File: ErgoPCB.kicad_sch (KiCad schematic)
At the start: 19 parts, among them J1 Conn_01x04_MountingPin, U1 STM32F072CBT6, U3 PRTR5V0U2X, U4 XC6206PxxxMR-Regulator_Linear

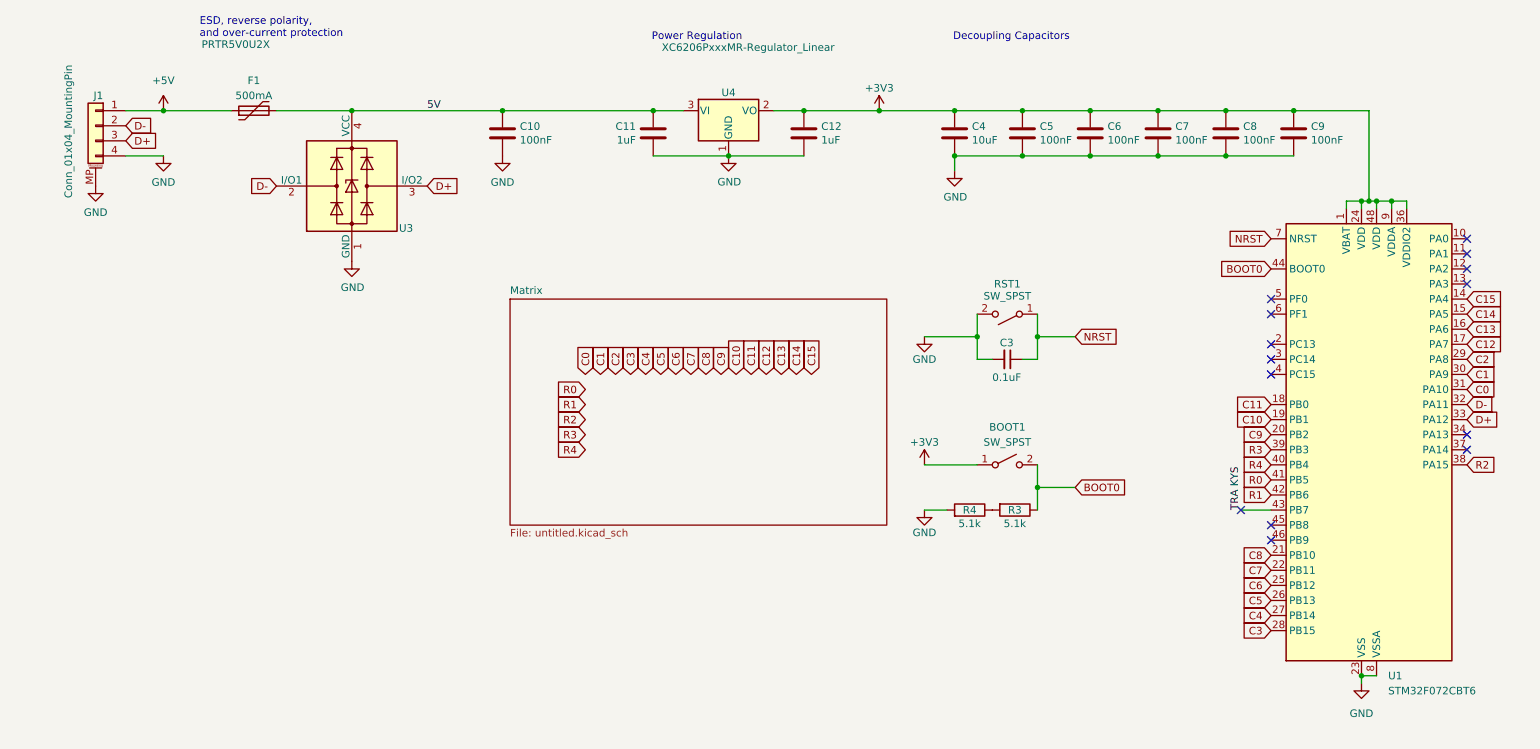
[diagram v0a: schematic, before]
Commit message: ESD protection change and redid decoupling capacitors
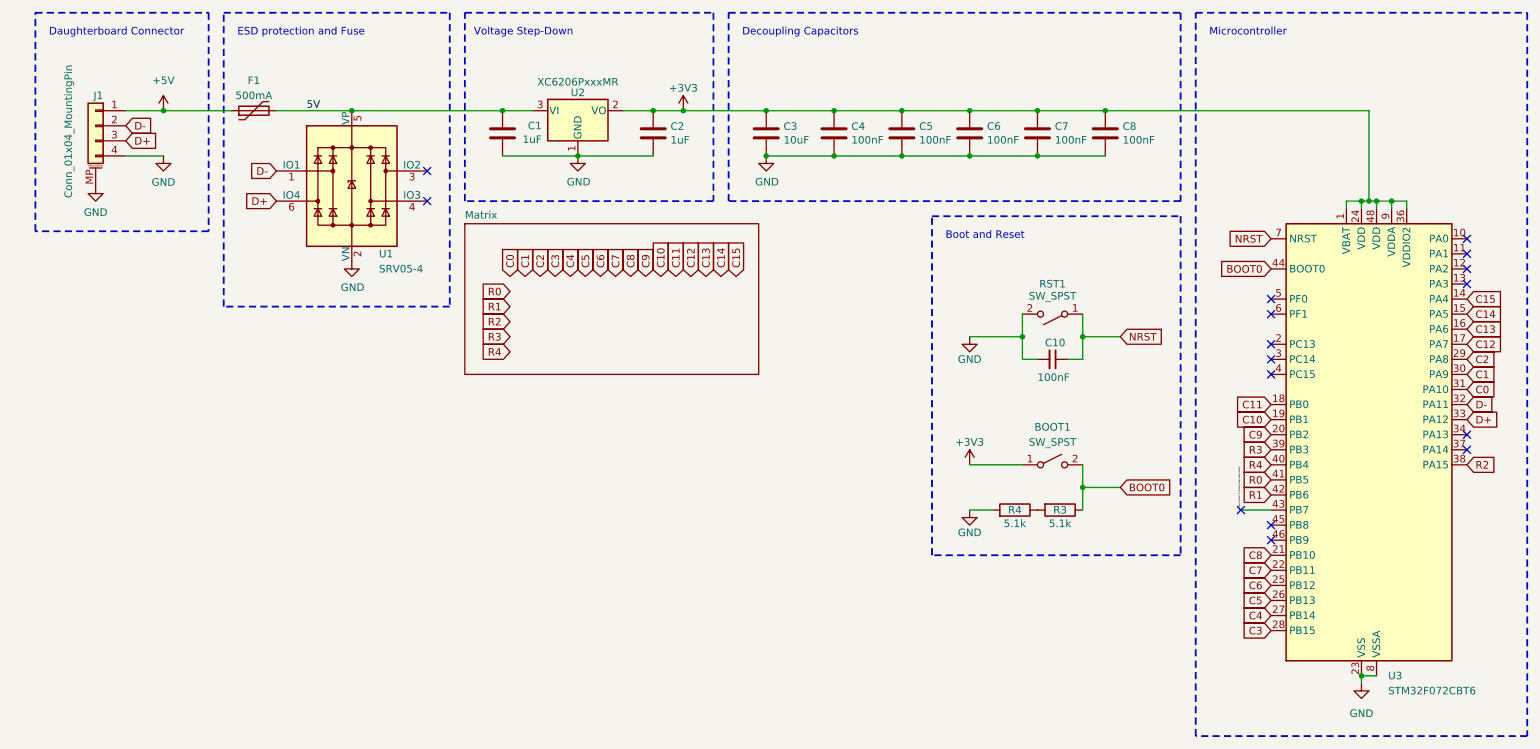
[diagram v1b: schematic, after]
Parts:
- removed C10: 100nF, Capacitor_SMD:C_0402_1005Metric, symbol Device:C
- removed U3: PRTR5V0U2X, Package_TO_SOT_SMD:SOT-143, symbol Power_Protection:PRTR5V0U2X
- added U1: SRV05-4, PCM_marbastlib-various:SOT-23-6-routable, symbol PCM_marbastlib-various:SRV05-4
- C10: renamed from C3; value 0.1uF -> 100nF
- U2: renamed from U4; value XC6206PxxxMR-Regulator_Linear -> XC6206PxxxMR
- renumbered C11 to C1, C12 to C2, C4 to C3, C5 to C4, C6 to C5, C7 to C6, C8 to C7, C9 to C8, U1 to U3
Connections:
- net 5V: now also U1.5 (VP)
- net D+: now also U1.6 (IO4)
- net D-: now also U1.1 (IO1)
- net GND: now also U1.2 (VN)
- net TRA KYS renamed pls dont connect to randon things again thanks
- no-connect marks 14 -> 16
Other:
- sheet Matrix: file untitled.kicad_sch -> Matrix.kicad_sch
- note added: "Boot and Reset"
- note added: "Daughterboard Connector"
- note added: "ESD protection and Fuse"
- note added: "Microcontroller"
- note added: "Voltage Step-Down"
- note removed: "ESD, reverse polarity, and over-current protection"
- note removed: "Power Regulation"
- moved on the sheet: BOOT1, C1, C10, C2, C3, C4, C5, C6, C7, C8, R3, R4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

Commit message: Small changes
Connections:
- net pls dont connect to randon things again thanks renamed     pls dont connect to randon things again thanks
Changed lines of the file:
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@@
 	)
 	(no_connect
-		(at 226.06 111.76)
+		(at 222.25 111.76)
 	)
 	(no_connect
@@
 	(wire
 		(pts
-			(xy 248.92 59.69) (xy 248.92 60.96)
+			(xy 222.25 111.76) (xy 231.14 111.76)
 		)
 		(stroke
@@
 	(wire
 		(pts
-			(xy 199.39 107.95) (xy 199.39 111.76)
+			(xy 248.92 59.69) (xy 248.92 60.96)
 		)
 		(stroke
@@
 	(wire
 		(pts
-			(xy 189.23 86.36) (xy 189.23 82.55)
+			(xy 199.39 107.95) (xy 199.39 111.76)
 		)
 		(stroke
@@
 	(wire
 		(pts
-			(xy 38.1 52.07) (xy 44.45 52.07)
+			(xy 189.23 86.36) (xy 189.23 82.55)
 		)
 		(stroke
@@
 	(wire
 		(pts
-			(xy 251.46 59.69) (xy 251.46 60.96)
+			(xy 38.1 52.07) (xy 44.45 52.07)
 		)
 		(stroke
@@
 	(wire
 		(pts
-			(xy 191.77 44.45) (xy 203.2 44.45)
+			(xy 251.46 59.69) (xy 251.46 60.96)
 		)
 		(stroke
@@
 	(wire
 		(pts
-			(xy 226.06 111.76) (xy 231.14 111.76)
+			(xy 191.77 44.45) (xy 203.2 44.45)
 		)
 		(stroke
@@
 		)
 	)
-	(label "pls dont connect to randon things again thanks"
-		(at 226.06 111.76 90)
+	(label "    pls dont connect to randon things again thanks"
+		(at 223.52 111.76 90)
 		(effects
 			(font
@@
 	)
 	(sheet
-		(at 95.25 63.5)
+		(at 95.25 62.23)
 		(size 49.53 25.4)
-		(fields_autoplaced yes)
 		(stroke
 			(width 0.15)
@@
 		)
 		(property "Sheetname" "Matrix"
-			(at 95.25 62.7884 0)
+			(at 96.266 66.04 0)
 			(effects
 				(font
@@
 		)
 		(property "Sheetfile" "Matrix.kicad_sch"
-			(at 95.25 89.4846 0)
+			(at 95.25 88.2146 0)
 			(effects
 				(font

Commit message: Small fixes
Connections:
- net 5V is gone; now on net +5V: C1.1, F1.2, U1.5 (VP), U2.3 (VI)
- net +5V: no longer F1.1, J1.1 (Pin_1)
- net D+: now also U1.3 (IO2), U1.4 (IO3); no longer U1.6 (IO4)
- net D-: now also U1.6 (IO4)
- new net VBUS: F1.1, J1.1 (Pin_1)
- no-connect marks 16 -> 14
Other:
- moved on the sheet: F1, J1, U1

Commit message: New molex connector footprint and 3V3 line to BOOT0 routed away from the BOOT and NRST traces
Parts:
- J1: footprint PCM_marbastlib-various:Molex_Pico-EZmate_78171-0004_1x04-1MP_P1.20mm_Vertical -> PCM_marbastlib-various:Molex_Pico-EZmate_78171-0004_1x04-1MP_P1.20mm_Vertical_No_Through_Hole
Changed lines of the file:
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@@
 			)
 		)
-		(property "Footprint" "PCM_marbastlib-various:Molex_Pico-EZmate_78171-0004_1x04-1MP_P1.20mm_Vertical"
+		(property "Footprint" "PCM_marbastlib-various:Molex_Pico-EZmate_78171-0004_1x04-1MP_P1.20mm_Vertical_No_Through_Hole"
 			(at 29.21 46.99 0)
 			(effects

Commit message: Changed to JST
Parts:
- J1: footprint PCM_marbastlib-various:Molex_Pico-EZmate_78171-0004_1x04-1MP_P1.20mm_Vertical_No_Through_Hole -> Connector_JST:JST_SH_SM04B-SRSS-TB_1x04-1MP_P1.00mm_Horizontal
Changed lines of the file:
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@@
 			)
 		)
-		(property "Footprint" "PCM_marbastlib-various:Molex_Pico-EZmate_78171-0004_1x04-1MP_P1.20mm_Vertical_No_Through_Hole"
+		(property "Footprint" "Connector_JST:JST_SH_SM04B-SRSS-TB_1x04-1MP_P1.00mm_Horizontal"
 			(at 29.21 46.99 0)
 			(effects
